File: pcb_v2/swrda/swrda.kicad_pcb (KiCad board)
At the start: 2 copper layers, 125.7 x 73 mm, 25 parts, among them J1 addr_decoder, U1 74LS138, U10 74LS32, U12 74LS02, U2 74LS138, U3 74LS138, U4 74LS138, U5 74LS04, U6 74LS08, U7 74LS00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

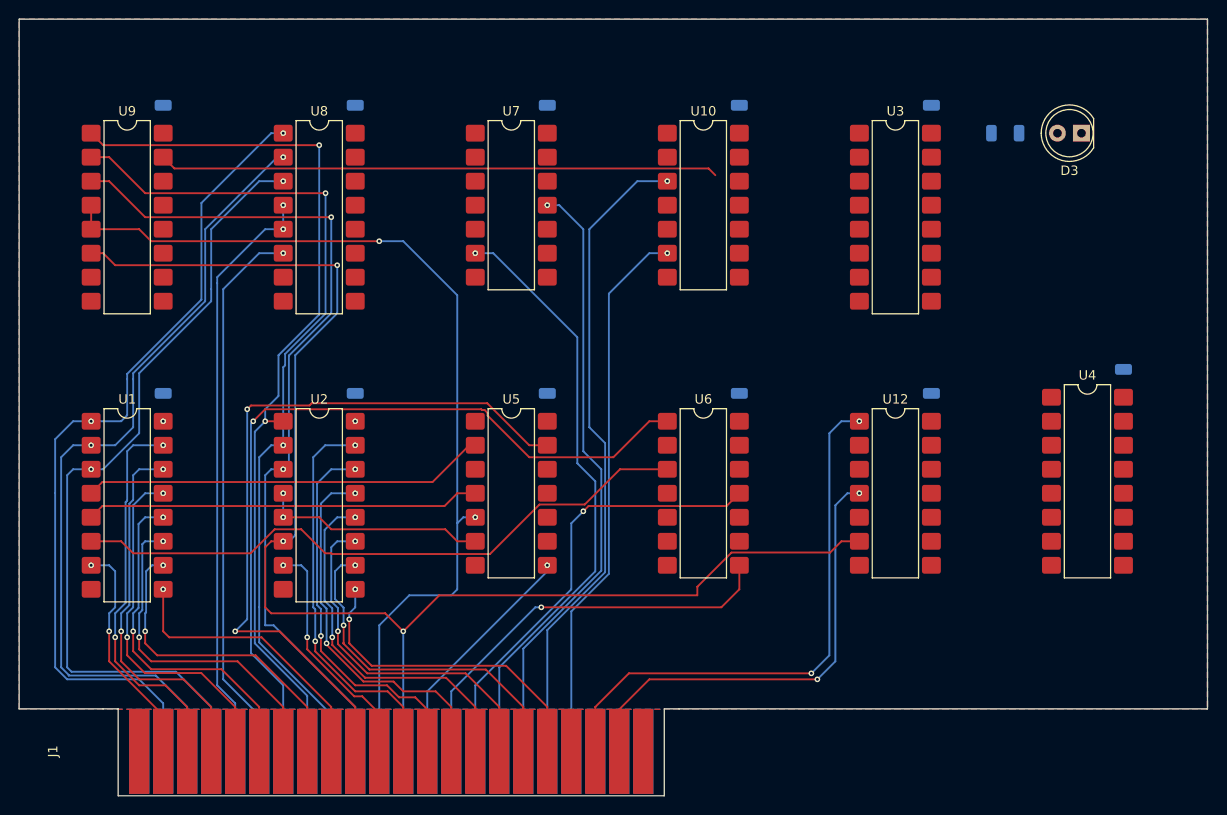
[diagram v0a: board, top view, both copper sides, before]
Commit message: roteamento pronto e electric rules verificadas
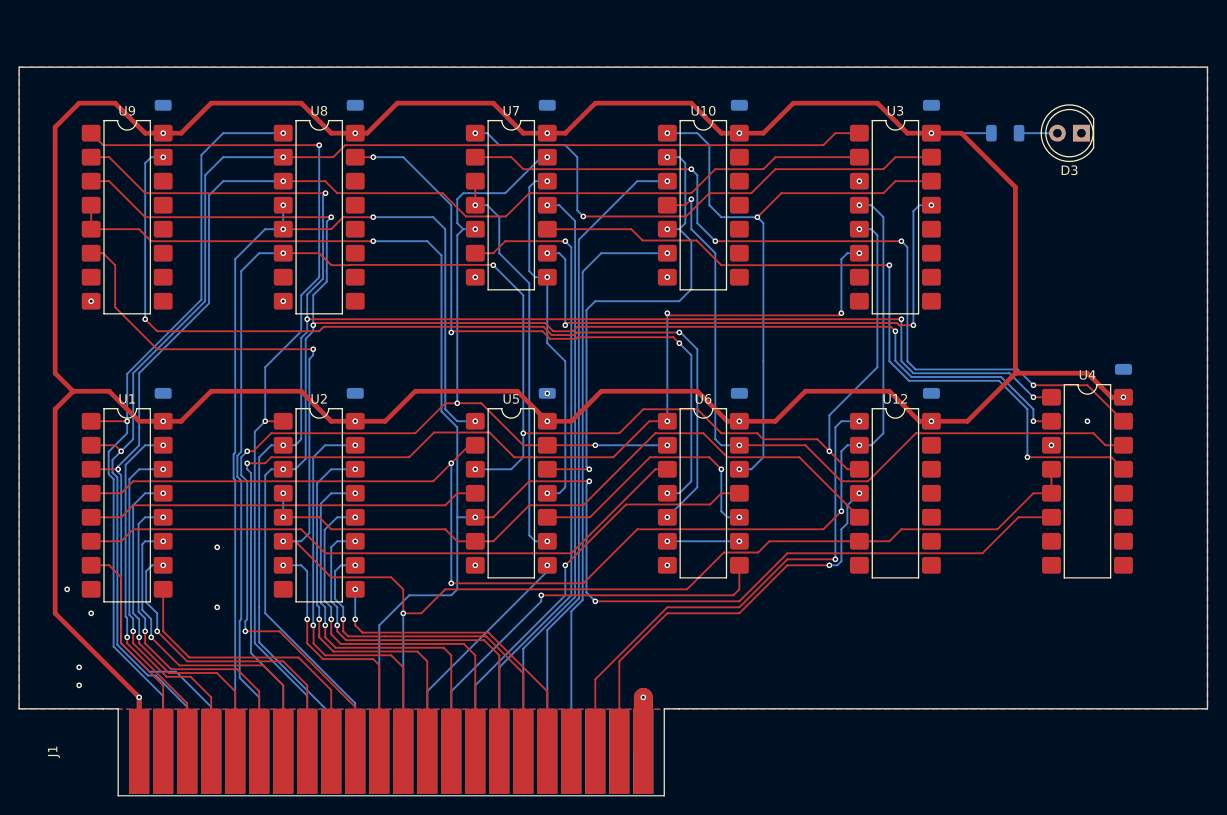
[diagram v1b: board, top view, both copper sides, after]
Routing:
- net +5V: track 0.00 -> 346.0 mm, vias 2 -> 12
- net wr_addr_4: track 58.4 -> 173.7 mm, vias 1 -> 6
- net ~{wr_addr_3}: track 42.7 -> 137.4 mm, vias 0 -> 5
- net ~{addr_read_pc}: track 0.00 -> 90.2 mm, vias 0 -> 4
- net rd_addr_2: track 91.6 -> 177.3 mm, vias 2 -> 5
- net rd_addr_1: track 92.2 -> 177.7 mm, vias 2 -> 5
- net ~{addr_read_mar}: track 0.00 -> 80.4 mm, vias 0 -> 2
- net rd_addr_3: track 100.6 -> 180.6 mm, vias 2 -> 4
- net ~{addr_read_sp}: track 0.00 -> 76.9 mm, vias 0 -> 2
- net ~{write_iod_mar}: track 0.00 -> 68.8 mm, vias 0 -> 4
- net ~{addr_write_sp}: track 0.00 -> 65.6 mm, vias 0 -> 3
- net ~{addr_write_mar}: track 0.00 -> 60.4 mm, vias 0 -> 4
- net wr_addr_2: track 85.9 -> 145.0 mm
- net ~{addr_write_pc}: track 0.00 -> 57.8 mm, vias 0 -> 2
- net wr_addr_1: track 86.5 -> 143.3 mm
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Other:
- board size 125.7 x 73 mm -> 125.7 x 67.9 mm

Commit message: concluido o desenho das placas satelite do banco de registradores de 16 bits
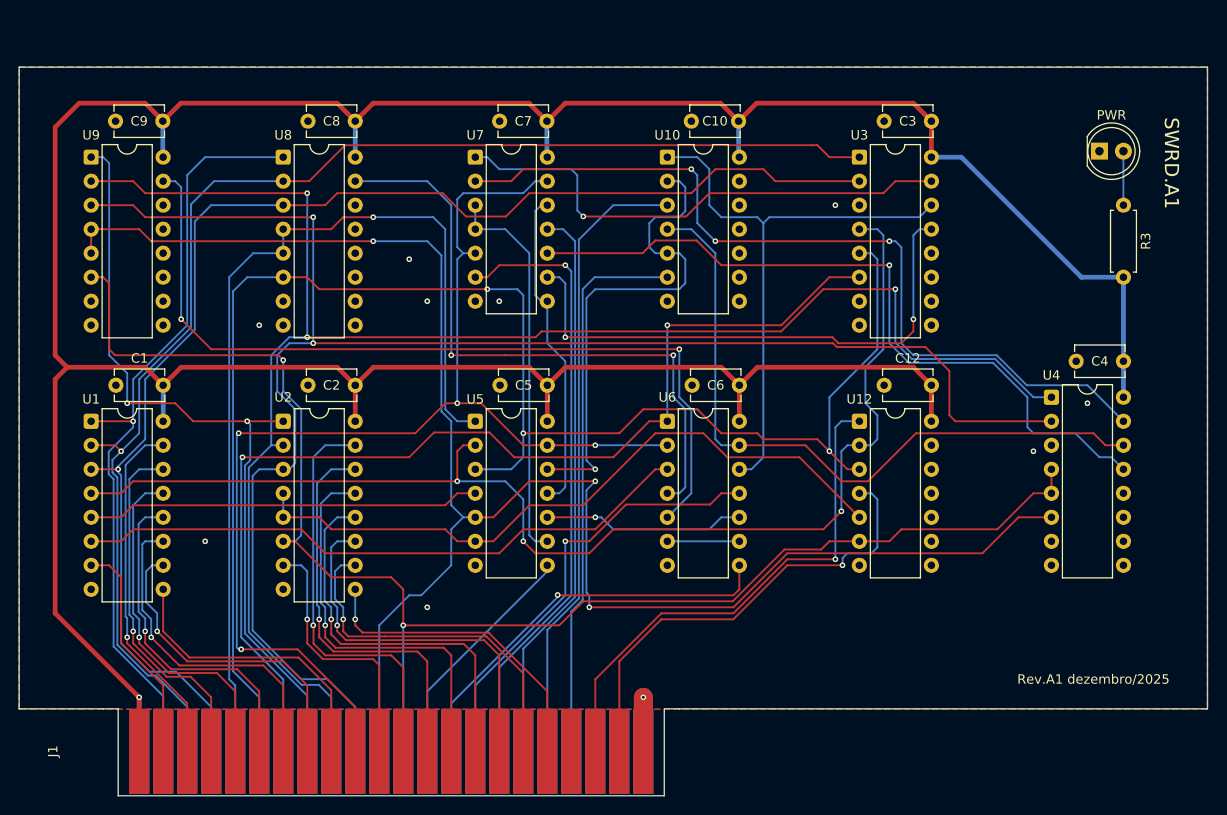
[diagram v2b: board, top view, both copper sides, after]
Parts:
- C1, C10, C12, C2, C3, C4, C5, C6, C7, C8, C9: footprint Capacitor_SMD:C_1206_3216Metric -> Capacitor_THT:C_Disc_D5.1mm_W3.2mm_P5.00mm; moved to F.Cu
- D3: value LED -> PWR
- R3: footprint Resistor_SMD:R_1206_3216Metric -> Resistor_THT:R_Axial_DIN0207_L6.3mm_D2.5mm_P7.62mm_Horizontal; moved to F.Cu
- U1, U2, U3, U4, U8, U9: footprint Package_DIP:SMDIP-16_W7.62mm -> Package_DIP:DIP-16_W7.62mm
- U10, U12, U5, U6, U7: footprint Package_DIP:SMDIP-14_W7.62mm -> Package_DIP:DIP-14_W7.62mm
- moved R3 14.6 mm to (157.5, 61.6), turned to -90 degrees
- moved U1 9.67 mm to (48.3, 84.5)
- moved U2 9.67 mm to (68.6, 84.5)
- moved U4 9.67 mm to (149.9, 81.9)
- moved U12 8.52 mm to (129.5, 84.5)
- moved U6 8.52 mm to (109.2, 84.5)
- moved U5 8.52 mm to (88.9, 84.5)
- moved U3 7.41 mm to (129.5, 56.5)
- moved U8 7.41 mm to (68.6, 56.5)
- moved U9 7.41 mm to (48.3, 56.5)
- moved U10 6.35 mm to (109.2, 56.5)
- moved U7 6.35 mm to (88.9, 56.5)
- moved C1 5.52 mm to (50.9, 80.6), turned to 0 degrees
- moved C12 5.52 mm to (132.2, 80.6), turned to 0 degrees
- moved C2 5.52 mm to (71.2, 80.6), turned to 0 degrees
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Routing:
- net rd_addr_0: track 95.8 -> 83.7 mm
- net ~{read_iod_mar}: track 98.1 -> 89.5 mm, vias 4 -> 2
- net ~{wr_addr_3}: track 137.4 -> 129.9 mm, vias 5 -> 3
- net +5V: track 346.0 -> 353.0 mm, vias 12 -> 1
- net Net-(U5-Pad10): track 28.2 -> 21.4 mm, vias 2 -> 1
- net wr_addr_4: track 173.7 -> 168.5 mm, vias 6 -> 3
- net wr_enable: track 118.4 -> 114.3 mm, vias 5 -> 2
- net memory_read: track 45.4 -> 49.5 mm, vias 2 -> 1
- net ~{addr_write_sp}: track 65.6 -> 61.7 mm, vias 3 -> 0
- net Net-(U5-Pad11): track 38.4 -> 34.6 mm, vias 3 -> 0
- net ~{addr_read_sp}: track 76.9 -> 73.5 mm, vias 2 -> 0
- net ~{addr_write_pc}: track 57.8 -> 54.6 mm, vias 2 -> 1
- net rd_addr_1: track 177.7 -> 180.9 mm, vias 5 -> 3
- net rd_addr_4: track 161.4 -> 158.4 mm, vias 3 -> 2
- net ~{addr_write_mar}: track 60.4 -> 57.8 mm, vias 4 -> 2
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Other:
- board text added: "Rev.A1 dezembro/2025"
- board text added: "SWRD.A1"
